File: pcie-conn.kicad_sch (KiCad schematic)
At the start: 22 parts

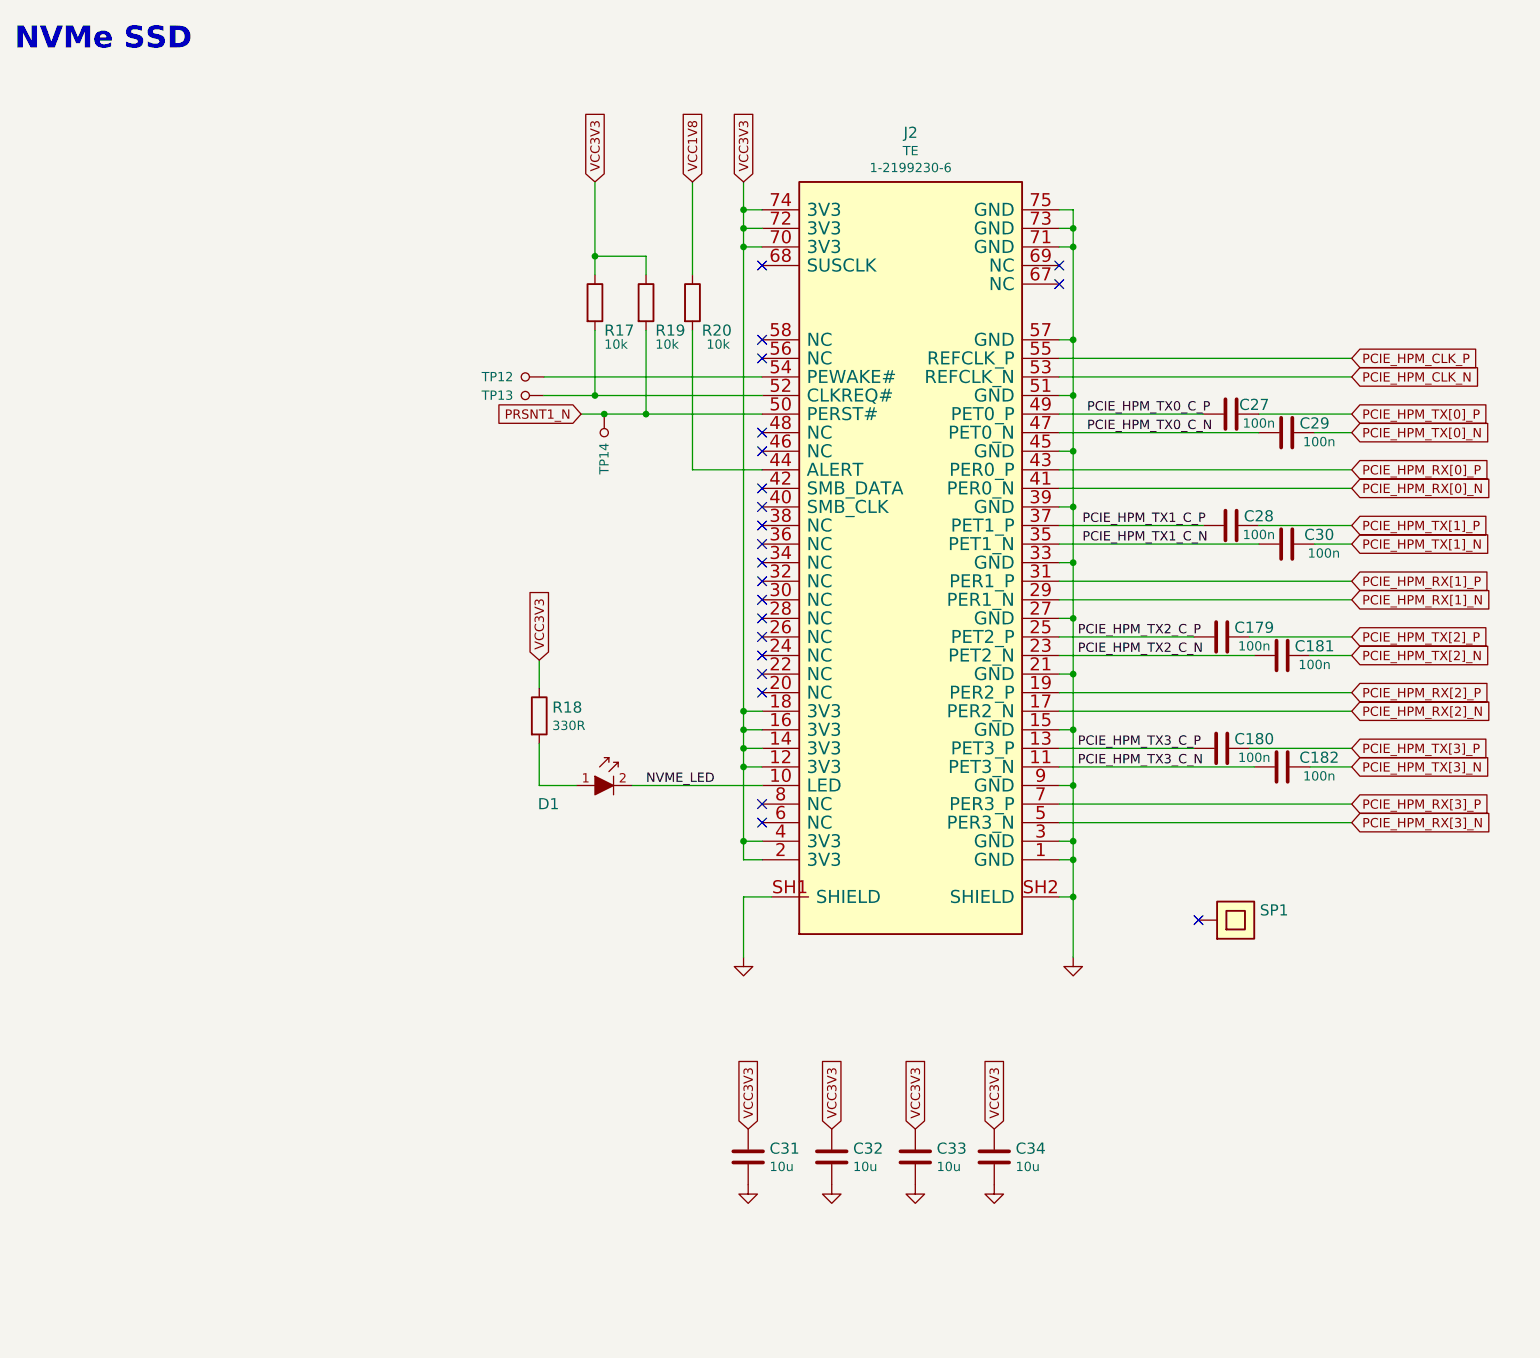
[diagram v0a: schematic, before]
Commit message: Introduce component standardization
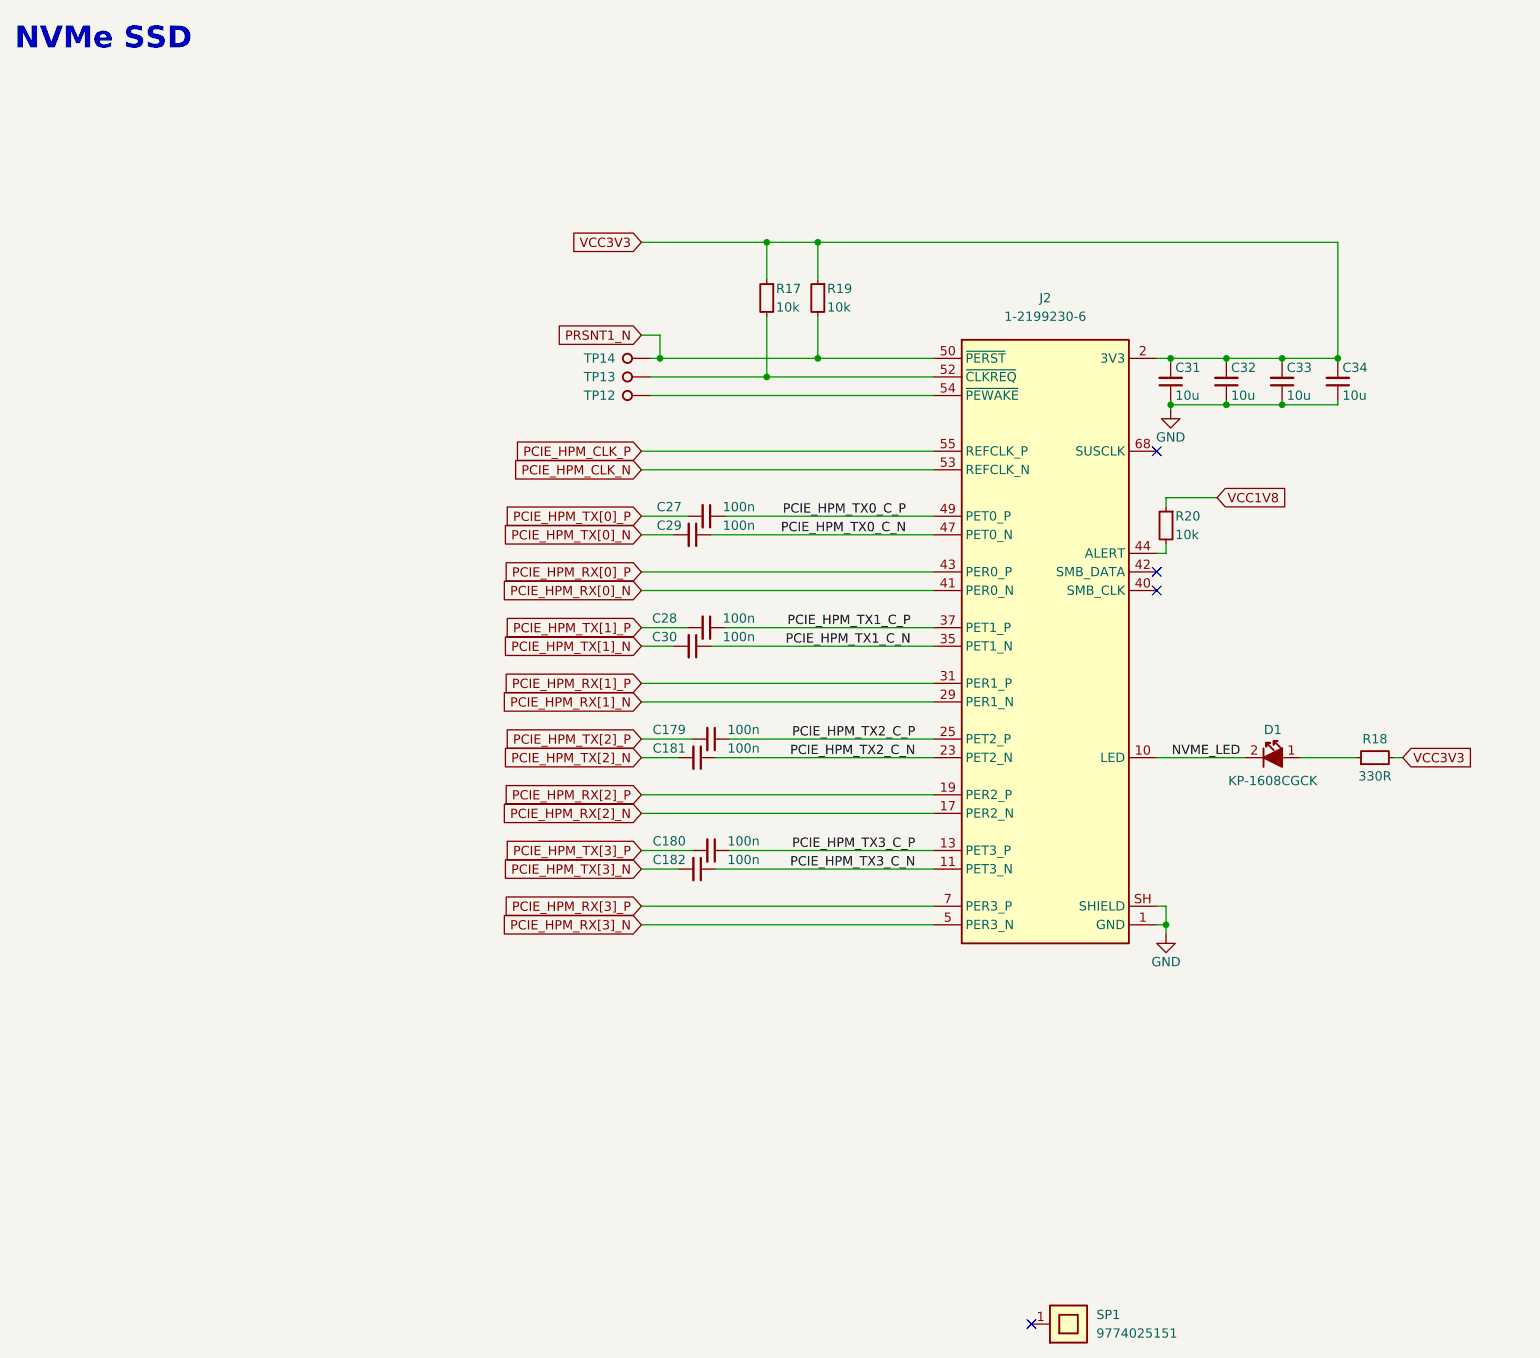
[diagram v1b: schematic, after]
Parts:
- C179, C180, C181, C182, C27, C28, C29, C30: value (none) -> C_100n_6V3_0402; footprint (none) -> antmicro-footprints:C_0402_1005Metric; symbol artix-dc-scm:C_100n_0402-artix-dc-scm -> antmicroCapacitorsmisc:C_100n_6V3_0402; Author (none) -> Antmicro; License (none) -> Apache-2.0
- C31, C32, C33, C34: value (none) -> C_10u_0402; footprint (none) -> antmicro-footprints:C_0402_1005Metric; symbol artix-dc-scm:C_10u_0402 -> antmicroCapacitors0402:C_10u_0402; Author (none) -> Antmicro; License (none) -> Apache-2.0; MPN GRM155R60J106ME44D -> CC0402MRX5R5BB106; Manufacturer MURATA -> Yaego
- D1: value (none) -> LED_G_0603_KP-1608CGCK; footprint (none) -> antmicro-footprints:LED_0603_1608Metric_G; symbol artix-dc-scm:KP-1608CGCK -> antmicroLEDIndicationDiscrete:LED_G_0603_KP-1608CGCK; Author (none) -> Antmicro; License (none) -> Apache-2.0; Manufacturer KINGBRIGHT -> Kingbright
- J2: value (none) -> Bus_M.2_1-2199230-6; footprint (none) -> antmicro-footprints:Bus_M.2_Socket_Key_M_TE_1-2199230-6; symbol artix-dc-scm:1-2199230-6 -> antmicroPciConnectors:Bus_M.2_1-2199230-6; Author (none) -> Antmicro; License (none) -> Apache-2.0; Manufacturer TE -> TE Connectivity
- R17, R19, R20: value (none) -> R_10k_0402; footprint (none) -> antmicro-footprints:R_0402_1005Metric; symbol artix-dc-scm:R_10k_0402 -> antmicroResistors0402:R_10k_0402; Author (none) -> Antmicro; License (none) -> Apache-2.0; MPN CRCW040210K0FKEDHP -> CR0402-FX-1002GLF; Manufacturer VISHAY -> Bourns; Tolerance (none) -> 1%
- R18: value (none) -> R_330R_0402; footprint (none) -> antmicro-footprints:R_0402_1005Metric; symbol artix-dc-scm:R_330R_0402 -> antmicroResistors0402:R_330R_0402; Author (none) -> Antmicro; License (none) -> Apache-2.0; MPN MCMR04X3300FTL -> CR0402-FX-3300GLF; Manufacturer MULTICOMP -> Bourns; Tolerance (none) -> 1%
- SP1: value (none) -> Spacer_H2.5mm_9774025151; footprint (none) -> antmicro-footprints:Spacer_SMD_M2.5_H2.5mm_Wurth_9774025151; symbol artix-dc-scm:9774025151 -> antmicroMechanicalParts:Spacer_H2.5mm_9774025151; Author (none) -> Antmicro; License (none) -> Apache-2.0; Manufacturer Wurth Elektronik -> Würth Elektronik
- TP12, TP13, TP14: value (none) -> TP_SMD1MM; footprint (none) -> antmicro-footprints:Testpoint_smd_1mm; symbol artix-dc-scm:TP_SMD1MM -> antmicroTestPoints:TP_1mm_SMD; Author (none) -> Antmicro; DNP (none) -> DNP; License (none) -> Apache-2.0
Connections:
- net GND: now also C31.1, C32.1, C33.1, C34.1, J2.SH (SHIELD); no longer C31.2, C32.2, C33.2, C34.2, J2.SH1 (SHIELD), J2.SH2 (SHIELD)
- net VCC3V3: now also C31.2, C32.2, C33.2, C34.2, R18.2; no longer C31.1, C32.1, C33.1, C34.1, R18.1
- net at D1.1: now also R18.1; no longer R18.2
- no-connect marks 22 -> 4
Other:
- moved on the sheet: C179, C180, C181, C182, C27, C28, C29, C30, C31, C32, C33, C34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

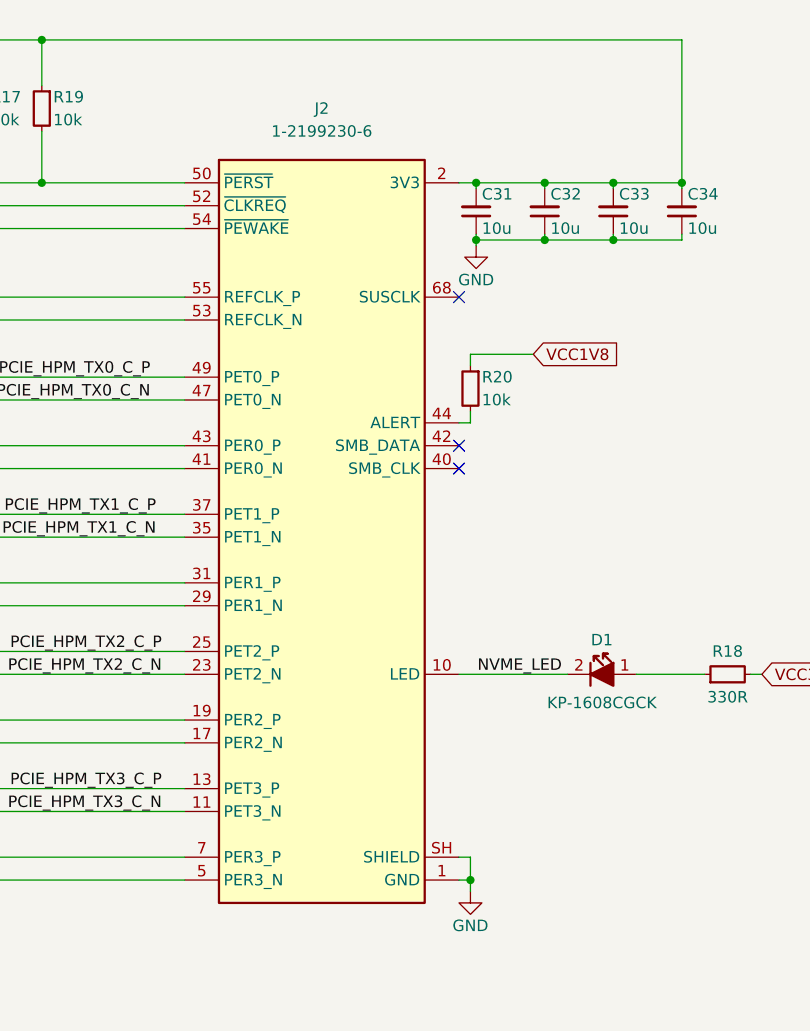
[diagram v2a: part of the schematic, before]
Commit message: Fix schematic ERC errors. ERC clean
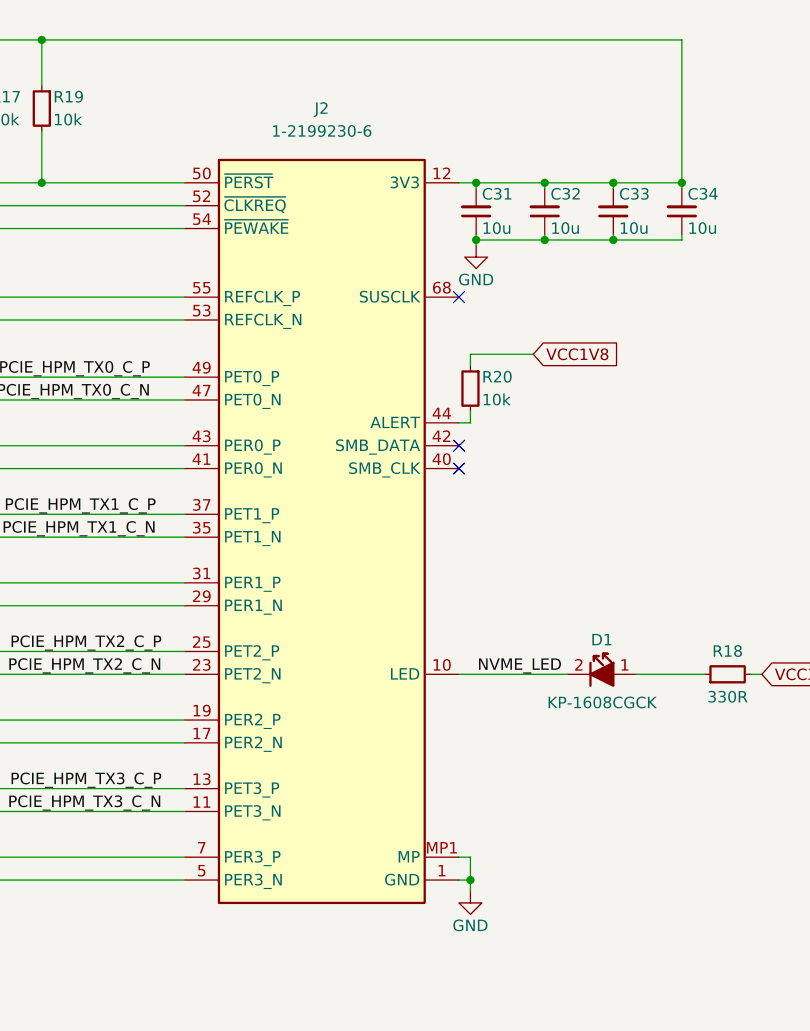
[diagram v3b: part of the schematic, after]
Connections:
- net GND: now also J2.MP1 (MP), J2.MP2 (MP); no longer J2.SH (SHIELD)
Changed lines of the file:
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@@
     (pin "8")
     (pin "9")
-    (pin "SH")
+    (pin "MP1")
+    (pin "MP2")
   )
   (symbol (lib_name "R_10k_0402_1") (lib_id "antmicroResistors0402:R_10k_0402") (at 118.745 51.435 270) (unit 1)
@@
       (effects (font (size 1.27 1.27)) hide)
     )
+    (property "Author" "Antmicro" (id 4) (at 182.245 148.59 0)
+      (effects (font (size 1.27 1.27) (thickness 0.15)) (justify left bottom) hide)
+    )
+    (property "License" "Apache-2.0" (id 5) (at 182.245 151.13 0)
+      (effects (font (size 1.27 1.27) (thickness 0.15)) (justify left bottom) hide)
+    )
     (pin "1")
   )
@@
       (effects (font (size 1.27 1.27)) hide)
     )
-    (pin "1")
+    (property "Author" "Antmicro" (id 4) (at 182.88 76.835 0)
+      (effects (font (size 1.27 1.27) (thickness 0.15)) (justify left bottom) hide)
+    )
+    (property "License" "Apache-2.0" (id 5) (at 182.88 79.375 0)
+      (effects (font (size 1.27 1.27) (thickness 0.15)) (justify left bottom) hide)
+    )
+    (pin "1")
